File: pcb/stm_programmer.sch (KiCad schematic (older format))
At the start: 37 parts

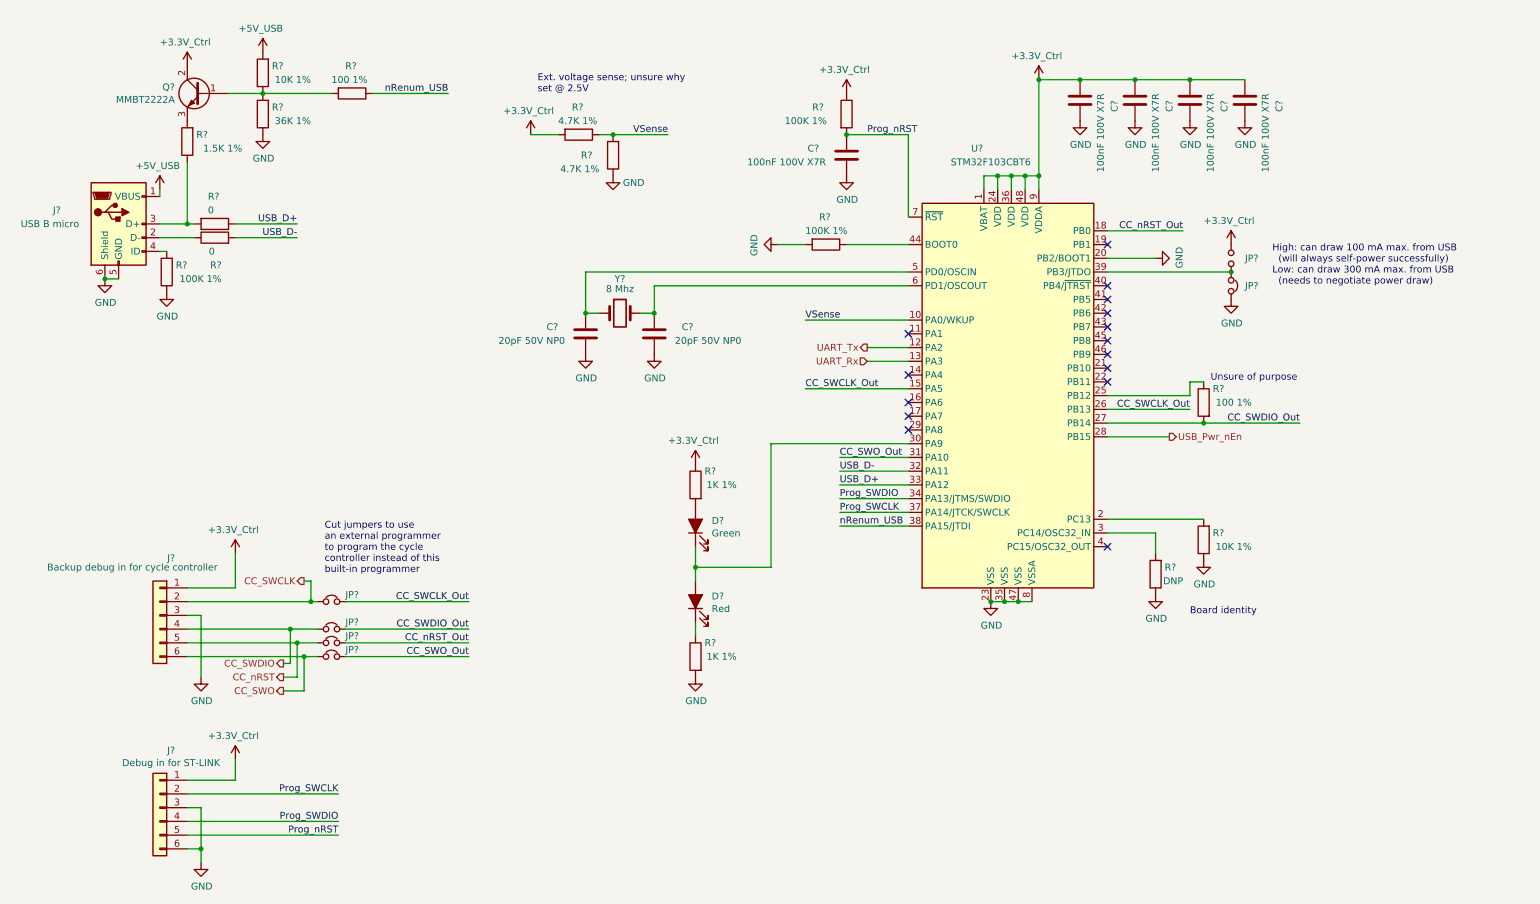
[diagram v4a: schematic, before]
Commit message: Top-level schematic (#1068)
* Cleanup

Added some extra useful KiCAD exclusions to gitignore
Removed project files and cache libraries that shouldn't have been present

* Cleanup cont.

* Top-level beginnings, minor fixes

Started on top-level schematic blocks and connections
Started changing some net names to mixed-case-with-dash format
Fixed version number, added titles and version to all schematic sheets
Fixed incorrect SWO pin assignment in cycle controller
Added a few add'l annotations to battery sheets

* Stepper drivers, alarms, power

Broke out SPI pins from cycle controller, routed to stepper drivers
Alarm/alarm battery changes:
(Fixed incorrect use of +BATT instead of +5V_Batt)
(Removed "run FPGA from alarm battery" circuitry and moved alarm battery circuitry to alarms sheet)
Converted fixed power symbols on logic/control power sheet, solenoid driver sheet to hierarchical labels to make power flow more clear from top level
Minor parts consolidation

* Monitoring

Finished top-level connections
Added separate SysMonADC for FPGA
Added voltage dividers for sensing input voltage levels
Broke out oxygen/temp sensor power to a hierarchical pin
Changed stepper STBY names to Reset to match ICD
Added OR'ed pull-downs to Stepper-nReset
Added FPGA alarm, external clamping for Low-Alarm-Bat signal
Added ability for FPGA to turn off 5V-UI
Changed CC's GND/GNDA connection from hardwired jumper to net tie
Added testpoints for probing

* Pinout fixes, TPs

Fixed pinout for stepper motor limit switches
Added testpoints to programmer's serial connection to CC

* CC-I2C, BOM

Added missing pull-ups on CC-SDA, CC-SCL
First pass at BOM consolidation

* BOM

More BOM consolidation with bulk capacitors + changed tantalum stepper caps to aluminum, added bulk cap to PSol driver
Made stepper's 3.3V power naming consistent with others (3.3V->3V3)
Slightly increased current limit on PSOL/heater driver
Changed 3906 transistors to 290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
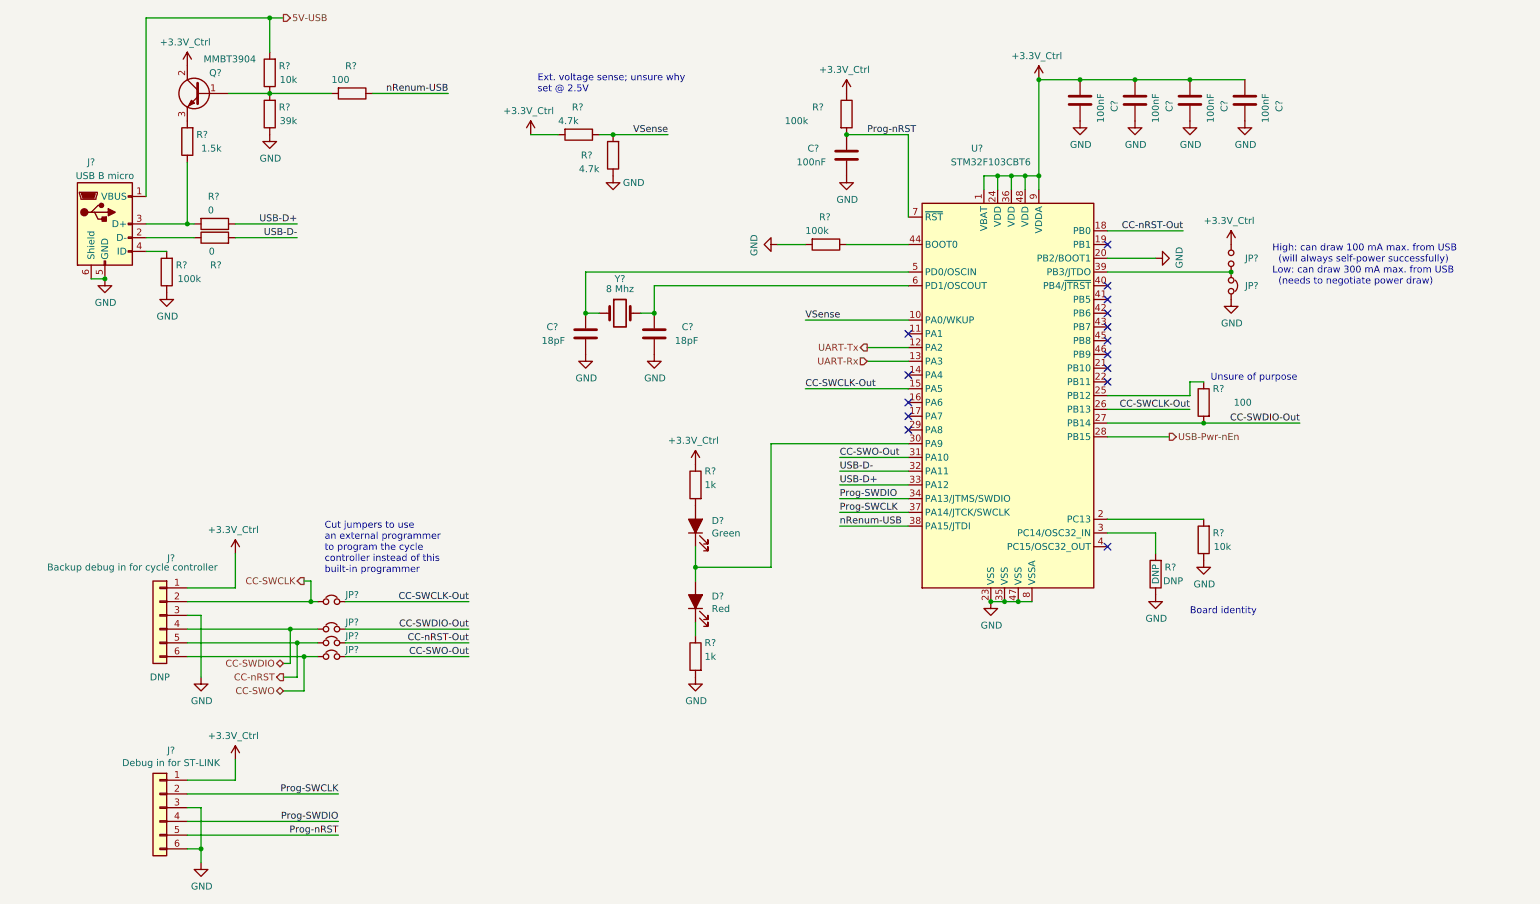
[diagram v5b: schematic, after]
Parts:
- C? (x5): value 100nF 100V X7R -> 100nF; Dielectric (none) -> X7R; Manufacturer (none) -> Kemet; Manufacturer PN (none) -> C0603C104K5RACTU; Voltage (none) -> 50V
- C? (x2): value 20pF 50V NP0 -> 18pF; Dielectric (none) -> NP0; Manufacturer (none) -> Kemet; Manufacturer PN (none) -> C0603C180J5GACTU; Voltage (none) -> 50V
- D?: footprint (none) -> RespiraWorks_Std:LED_0805_2012Metric; Manufacturer (none) -> Lite-On; Manufacturer PN (none) -> LTST-C170KRKT
- D?: footprint (none) -> RespiraWorks_Std:LED_0805_2012Metric; Manufacturer (none) -> Lite-On; Manufacturer PN (none) -> LTST-C171KGKT
- J?: footprint (none) -> RespiraWorks_Std:USB_Mini-B_Wuerth_65100516121_Horizontal; Manufacturer (none) -> Wuerth Elektronik; Manufacturer PN (none) -> 65100516121
- J?: footprint (none) -> RespiraWorks_Std:PinHeader_1x06_P2.54mm_Vertical; DNP (none) -> DNP; Manufacturer (none) -> Harwin; Manufacturer PN (none) -> M20-9980345
- J?: footprint (none) -> RespiraWorks_Std:PinHeader_1x06_P2.54mm_Vertical; Manufacturer (none) -> Harwin; Manufacturer PN (none) -> M20-9980345
- Q?: value MMBT2222A -> MMBT3904; Manufacturer (none) -> Diodes Inc.; Manufacturer PN (none) -> MMBT3904-7-F
- R? (x3): value 100K 1% -> 100k
- R? (x2): value 100 1% -> 100
- R?: value 1.5K 1% -> 1.5k
- R? (x2): value 10K 1% -> 10k
- R?: value 36K 1% -> 39k
- R? (x2): value 1K 1% -> 1k
- R? (x2): value 4.7K 1% -> 4.7k
- R?: DNP (none) -> DNP
- U?: Manufacturer (none) -> STMicroelectronics; Manufacturer PN (none) -> STM32F103CBT6
- Y?: Manufacturer (none) -> Abracon; Manufacturer PN (none) -> ABLS-8.000MHZ-B4-T
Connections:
- net +5V_USB renamed 5V-USB
- net CC_SWCLK renamed CC-SWCLK
- net CC_SWCLK_Out renamed CC-SWCLK-Out
- net CC_SWDIO renamed CC-SWDIO
- net CC_SWDIO_Out renamed CC-SWDIO-Out
- net CC_SWO renamed CC-SWO
- net CC_SWO_Out renamed CC-SWO-Out
- net CC_nRST renamed CC-nRST
- net CC_nRST_Out renamed CC-nRST-Out
- net Prog_SWCLK renamed Prog-SWCLK
- net Prog_SWDIO renamed Prog-SWDIO
- net Prog_nRST renamed Prog-nRST
- net UART_Rx renamed UART-Rx
- net UART_Tx renamed UART-Tx
- net USB_D+ renamed USB-D+
- net USB_D- renamed USB-D-
- net USB_Pwr_nEn renamed USB-Pwr-nEn
- net nRenum_USB renamed nRenum-USB
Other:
- moved on the sheet: J?, R?

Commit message: PCB Rev A Floorplanning (#1079)
* annotate schematics

* generate netlist

* define board edges at 150x300mm

* add parts to board (some pending errors)

* fix schem-pcb footprint mismatches and push to PCB

* preliminary packing at 155x300mm board size - marginal

* PCB floor planning

* added fan power and swapped solenoid/touchscreen power to vertical connectors
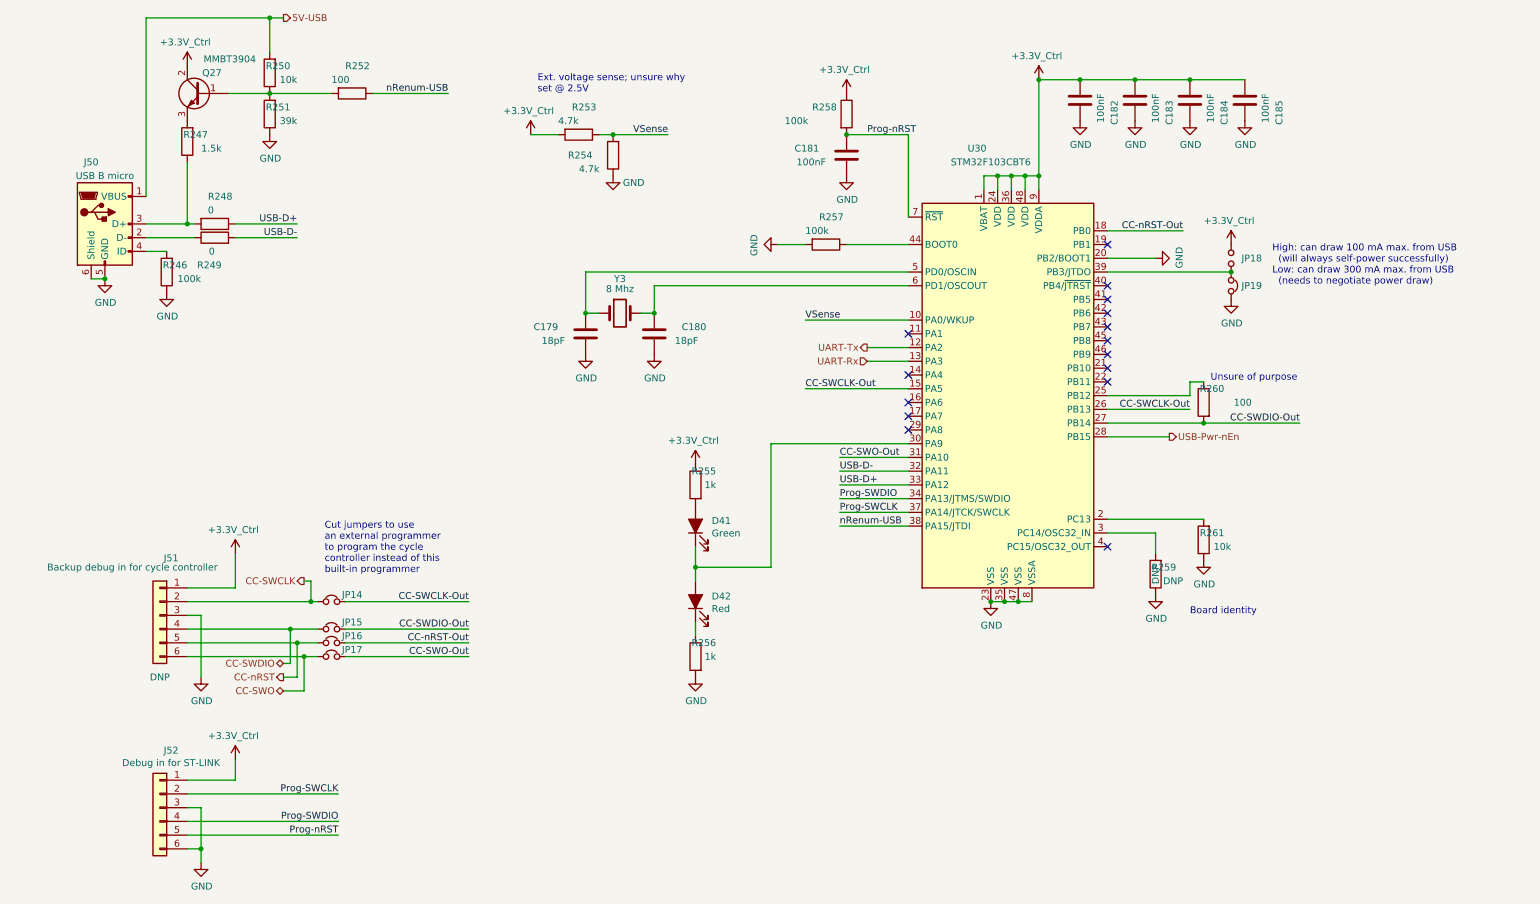
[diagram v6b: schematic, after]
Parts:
- gave numbers to parts that had none: 37

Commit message: PCB layout prep
Fixed incorrect pin assignments for BJTs
Fixed incorrect power symbol on alarms page
Set up default trace, via sizes
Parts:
- Q27: symbol Device:Q_NPN_BCE -> Device:Q_NPN_BEC
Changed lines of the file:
@@
 Connection ~ 1750 2500
 $Comp
-L Device:Q_NPN_BCE Q27
+L Device:Q_NPN_BEC Q27
 U 1 1 5FF31A97
 P 1850 1550

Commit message: Placement: alarms, solenoid drivers, O2/temp sensors, ST-Link
Initial placements, minor routing for testing route-ability
Fixed incorrect footprint for Raspberry Pi connector
Adjusted schematic positioning of values, references as necessary
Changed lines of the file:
@@
 AR Path="/5FCD4B8E/5FE27F70/5FF0A33E" Ref="R?"  Part="1"
 AR Path="/5FCD4D85/5FF0A33E" Ref="R260"  Part="1"
-F 0 "R260" H 9000 3900 50  0000 L CNN
-F 1 "100" H 8800 3800 50  0000 L CNN
+F 0 "R260" H 8850 3900 50  0000 L CNN
+F 1 "100" H 8900 3800 50  0000 L CNN
 F 2 "RespiraWorks_Std:R_0603_1608Metric" V 9080 3800 50  0001 C CNN
 F 3 "~" H 9150 3800 50  0001 C CNN
@@
 AR Path="/5FCD4B8E/5FE27F70/5FF24FD8" Ref="R?"  Part="1"
 AR Path="/5FCD4D85/5FF24FD8" Ref="R246"  Part="1"
-F 0 "R246" H 1450 2800 50  0000 L CNN
+F 0 "R246" H 1350 2800 50  0000 L CNN
 F 1 "100k" H 1350 2900 50  0000 L CNN
 F 2 "RespiraWorks_Std:R_0603_1608Metric" V 1530 2850 50  0001 C CNN
@@
 AR Path="/5FCD4B8E/5FE27F70/5FF27747" Ref="R?"  Part="1"
 AR Path="/5FCD4D85/5FF27747" Ref="R249"  Part="1"
-F 0 "R249" V 1750 2550 50  0000 L CNN
-F 1 "0" V 1850 2600 50  0000 L CNN
+F 0 "R249" V 1750 2400 50  0000 L CNN
+F 1 "0" V 1850 2550 50  0000 L CNN
 F 2 "RespiraWorks_Std:R_0603_1608Metric" V 1880 2600 50  0001 C CNN
 F 3 "~" H 1950 2600 50  0001 C CNN
@@
 AR Path="/5FCD4B8E/5FE27F70/5FF302E3" Ref="R?"  Part="1"
 AR Path="/5FCD4D85/5FF302E3" Ref="R247"  Part="1"
-F 0 "R247" H 1600 1850 50  0000 L CNN
+F 0 "R247" H 1500 1850 50  0000 L CNN
 F 1 "1.5k" H 1500 1950 50  0000 L CNN
 F 2 "RespiraWorks_Std:R_0603_1608Metric" V 1680 1900 50  0001 C CNN
@@
 AR Path="/5FCD4B8E/5FE27F70/5FF3BDCF" Ref="R?"  Part="1"
 AR Path="/5FCD4D85/5FF3BDCF" Ref="R250"  Part="1"
-F 0 "R250" H 2200 1350 50  0000 L CNN
+F 0 "R250" H 2100 1350 50  0000 L CNN
 F 1 "10k" H 2150 1450 50  0000 L CNN
 F 2 "RespiraWorks_Std:R_0603_1608Metric" V 2280 1400 50  0001 C CNN
@@
 AR Path="/5FCD4B8E/5FE27F70/5FF3C26A" Ref="R?"  Part="1"
 AR Path="/5FCD4D85/5FF3C26A" Ref="R251"  Part="1"
-F 0 "R251" H 2200 1650 50  0000 L CNN
+F 0 "R251" H 2100 1650 50  0000 L CNN
 F 1 "39k" H 2150 1750 50  0000 L CNN
 F 2 "RespiraWorks_Std:R_0603_1608Metric" V 2280 1700 50  0001 C CNN
@@
 AR Path="/5FCD4B8E/5FE27F70/5FF418B2" Ref="R?"  Part="1"
 AR Path="/5FCD4D85/5FF418B2" Ref="R252"  Part="1"
-F 0 "R252" V 2750 1500 50  0000 L CNN
-F 1 "100" V 2850 1400 50  0000 L CNN
+F 0 "R252" V 2750 1450 50  0000 L CNN
+F 1 "100" V 2850 1450 50  0000 L CNN
 F 2 "RespiraWorks_Std:R_0603_1608Metric" V 2880 1550 50  0001 C CNN
 F 3 "~" H 2950 1550 50  0001 C CNN
@@
 AR Path="/5FCD4B8E/5FE27F70/5FF56FF1" Ref="C?"  Part="1"
 AR Path="/5FCD4D85/5FF56FF1" Ref="C179"  Part="1"
-F 0 "C179" H 4850 3250 50  0000 L CNN
+F 0 "C179" H 4800 3250 50  0000 L CNN
 F 1 "18pF" H 4800 3350 50  0000 L CNN
 F 2 "RespiraWorks_Std:C_0603_1608Metric" H 4688 3150 50  0001 C CNN
@@
 AR Path="/5FCD4B8E/5FE27F70/5FF5ADBF" Ref="C?"  Part="1"
 AR Path="/5FCD4D85/5FF5ADBF" Ref="C180"  Part="1"
-F 0 "C180" H 5350 3250 50  0000 L CNN
+F 0 "C180" H 5300 3250 50  0000 L CNN
 F 1 "18pF" H 5300 3350 50  0000 L CNN
 F 2 "RespiraWorks_Std:C_0603_1608Metric" H 5188 3150 50  0001 C CNN
@@
 AR Path="/5FCD4B8E/5FE27F70/5FFEED71" Ref="R?"  Part="1"
 AR Path="/5FCD4D85/5FFEED71" Ref="R255"  Part="1"
-F 0 "R255" H 5300 4500 50  0000 L CNN
+F 0 "R255" H 5200 4500 50  0000 L CNN
 F 1 "1k" H 5300 4400 50  0000 L CNN
 F 2 "RespiraWorks_Std:R_0603_1608Metric" V 5380 4400 50  0001 C CNN
@@
 AR Path="/5FCD4B8E/5FE27F70/5FFEF31C" Ref="R?"  Part="1"
 AR Path="/5FCD4D85/5FFEF31C" Ref="R256"  Part="1"
-F 0 "R256" H 5300 5750 50  0000 L CNN
+F 0 "R256" H 5200 5750 50  0000 L CNN
 F 1 "1k" H 5300 5650 50  0000 L CNN
 F 2 "RespiraWorks_Std:R_0603_1608Metric" V 5380 5650 50  0001 C CNN
@@
 AR Path="/5FCD4D85/60068022" Ref="R253"  Part="1"
 F 0 "R253" V 4400 1800 50  0000 L CNN
-F 1 "4.7k" V 4500 1700 50  0000 L CNN
+F 1 "4.7k" V 4500 1800 50  0000 L CNN
 F 2 "RespiraWorks_Std:R_0603_1608Metric" V 4530 1850 50  0001 C CNN
 F 3 "~" H 4600 1850 50  0001 C CNN
@@
 AR Path="/5FCD4B8E/5FE27F70/600684BF" Ref="R?"  Part="1"
 AR Path="/5FCD4D85/600684BF" Ref="R254"  Part="1"
-F 0 "R254" H 5000 2000 50  0000 L CNN
-F 1 "4.7k" H 4950 2100 50  0000 L CNN
+F 0 "R254" H 4550 2000 50  0000 L CNN
+F 1 "4.7k" H 4600 2100 50  0000 L CNN
 F 2 "RespiraWorks_Std:R_0603_1608Metric" V 4780 2000 50  0001 C CNN
 F 3 "~" H 4850 2000 50  0001 C CNN
@@
 AR Path="/5FCD4B8E/5FE27F70/6007ED35" Ref="R?"  Part="1"
 AR Path="/5FCD4D85/6007ED35" Ref="R261"  Part="1"
-F 0 "R261" H 9000 4750 50  0000 L CNN
+F 0 "R261" H 8900 4750 50  0000 L CNN
 F 1 "10k" H 8950 4850 50  0000 L CNN
 F 2 "RespiraWorks_Std:R_0603_1608Metric" V 9080 4800 50  0001 C CNN
@@
 AR Path="/5FCD4B8E/5FE27F70/60080C40" Ref="R?"  Part="1"
 AR Path="/5FCD4D85/60080C40" Ref="R259"  Part="1"
-F 0 "R259" H 8650 5000 50  0000 L CNN
+F 0 "R259" H 8550 5000 50  0000 L CNN
 F 1 "DNP" H 8600 5100 50  0000 L CNN
 F 2 "RespiraWorks_Std:R_0603_1608Metric" V 8730 5050 50  0001 C CNN
